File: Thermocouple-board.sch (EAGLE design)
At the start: 78 parts, among them J1 RJ45, J11 1X2-3.5MM, J12 1X2-3.5MM, J13 1X2-3.5MM, J14 1X2-3.5MM, J2 RJ45, J3 1981584-1, J4 2.1MMJACKTHM, J5 ST-LINK, J6 HEADER-1X3, J7 HEADER-1X2, SW1 PUSHBUTTON, SW2 PUSHBUTTON, U1 STM32F042K4, U10 MAX31855, U11 MAX31855, U12 MAX31855, U13 MAX31855, U20 EEPROM-I2C, U21 EEPROM-I2C, U30 ST3485, U31 ST3485, U40 LP298XS, X1 NX3225GD

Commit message: WIP on larger MTG holes
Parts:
- added MH1, MH2, MH3, MH4: 4-40, Thermocouple-board:MTG_HOLE_4-40
- added U$3, U$6: MOUNTINGHOLE2.0, microbuilder:MOUNTINGHOLE2.0
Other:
- note added: "CENTER POSITIVE"
- note removed: "PWR ONLY"
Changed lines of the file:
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@@
 <part name="J6" library="Thermocouple-board" deviceset="HEADER-1X3" device=""/>
 <part name="C42" library="adafruit" deviceset="C-US" device="C0805K" value="10uF"/>
+<part name="MH1" library="Thermocouple-board" deviceset="MTG_HOLE" device="_4-40" value="4-40"/>
+<part name="MH2" library="Thermocouple-board" deviceset="MTG_HOLE" device="_4-40" value="4-40"/>
+<part name="MH3" library="Thermocouple-board" deviceset="MTG_HOLE" device="_4-40" value="4-40"/>
+<part name="MH4" library="Thermocouple-board" deviceset="MTG_HOLE" device="_4-40" value="4-40"/>
+<part name="U$3" library="microbuilder" deviceset="MOUNTINGHOLE" device="2.0"/>
+<part name="U$6" library="microbuilder" deviceset="MOUNTINGHOLE" device="2.0"/>
 </parts>
 <sheets>
@@
 8. DC-</text>
 <text x="-43.18" y="101.6" size="1.778" layer="91">ETHERNET</text>
-<text x="147.32" y="147.32" size="1.778" layer="91">PWR ONLY</text>
 <text x="73.66" y="127" size="1.778" layer="91">MTG HOLES</text>
 <text x="40.64" y="132.08" size="1.778" layer="91">POWER SELECT</text>
+<text x="-25.4" y="132.08" size="1.778" layer="91">CENTER POSITIVE</text>
 </plain>
 <instances>
@@
 <attribute name="VALUE" x="28.956" y="38.989" size="1.778" layer="96"/>
 </instance>
+<instance part="MH1" gate="G$1" x="88.9" y="121.92" smashed="yes">
+<attribute name="NAME" x="86.36" y="125.73" size="1.27" layer="95"/>
+<attribute name="VALUE" x="86.36" y="116.84" size="1.27" layer="96"/>
+</instance>
+<instance part="MH2" gate="G$1" x="96.52" y="121.92" smashed="yes">
+<attribute name="NAME" x="93.98" y="125.73" size="1.27" layer="95"/>
+<attribute name="VALUE" x="93.98" y="116.84" size="1.27" layer="96"/>
+</instance>
+<instance part="MH3" gate="G$1" x="104.14" y="121.92" smashed="yes">
+<attribute name="NAME" x="101.6" y="125.73" size="1.27" layer="95"/>
+<attribute name="VALUE" x="101.6" y="116.84" size="1.27" layer="96"/>
+</instance>
+<instance part="MH4" gate="G$1" x="111.76" y="121.92" smashed="yes">
+<attribute name="NAME" x="109.22" y="125.73" size="1.27" layer="95"/>
+<attribute name="VALUE" x="109.22" y="116.84" size="1.27" layer="96"/>
+</instance>
+<instance part="U$3" gate="G$1" x="76.2" y="111.76" smashed="yes"/>
+<instance part="U$6" gate="G$1" x="81.28" y="111.76" smashed="yes"/>
 </instances>
 <busses>

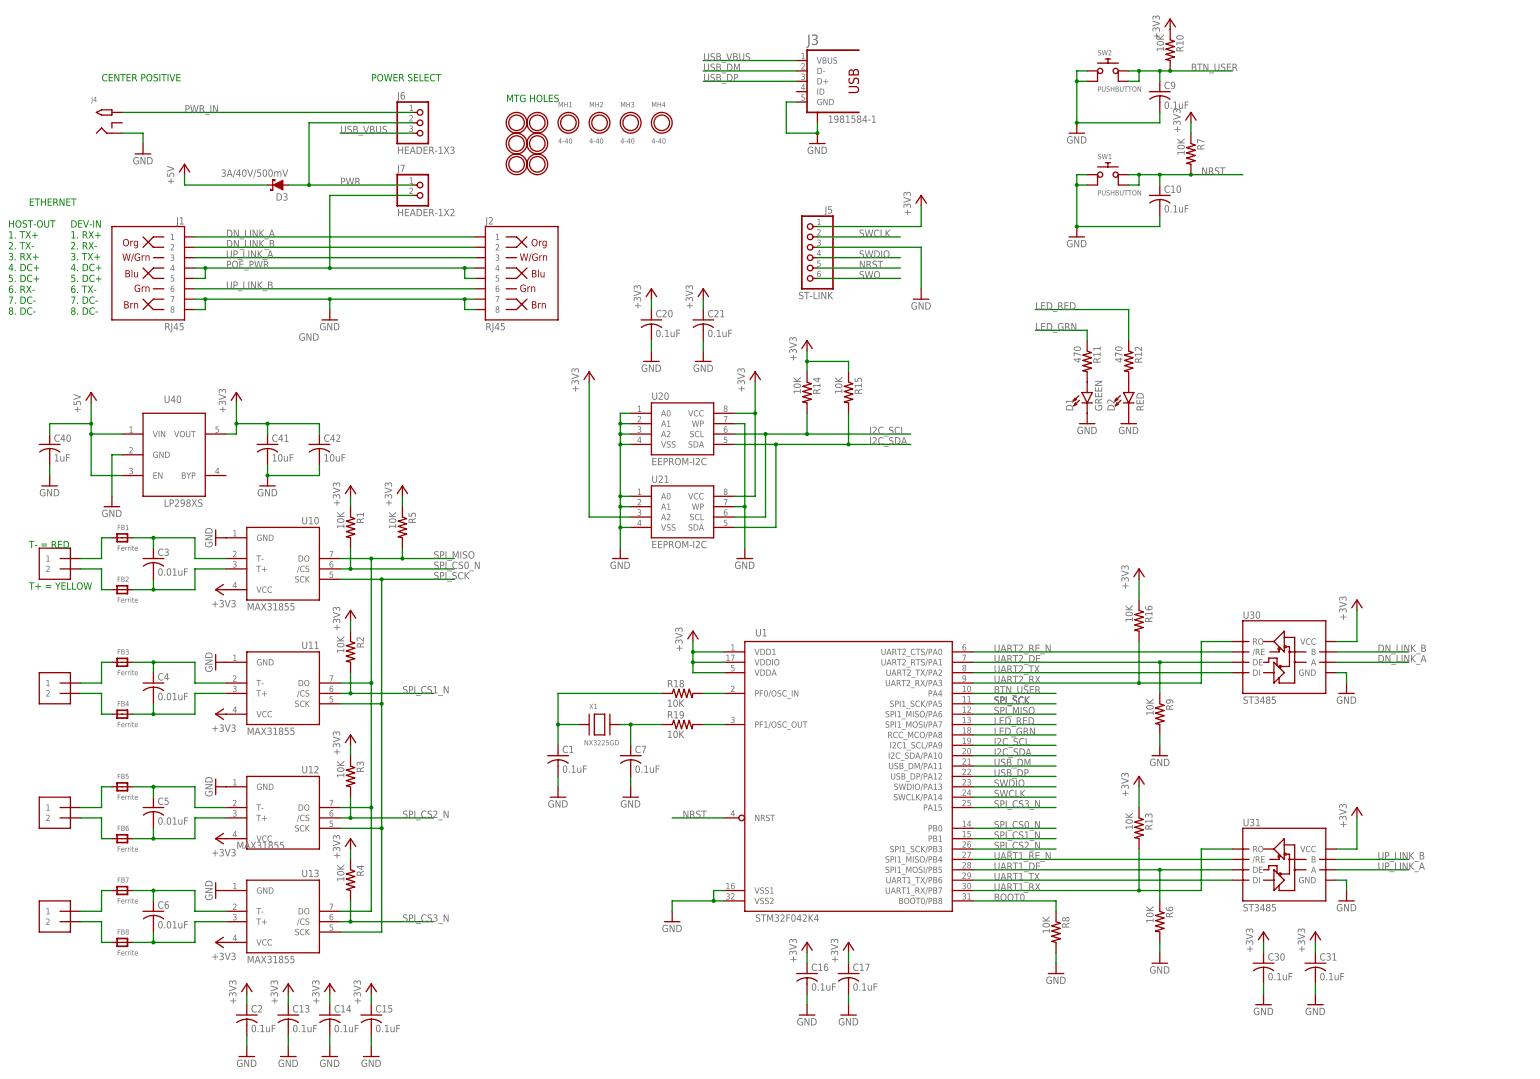
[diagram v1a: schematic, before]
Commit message: Reconfigured UARTs for FTDI cable
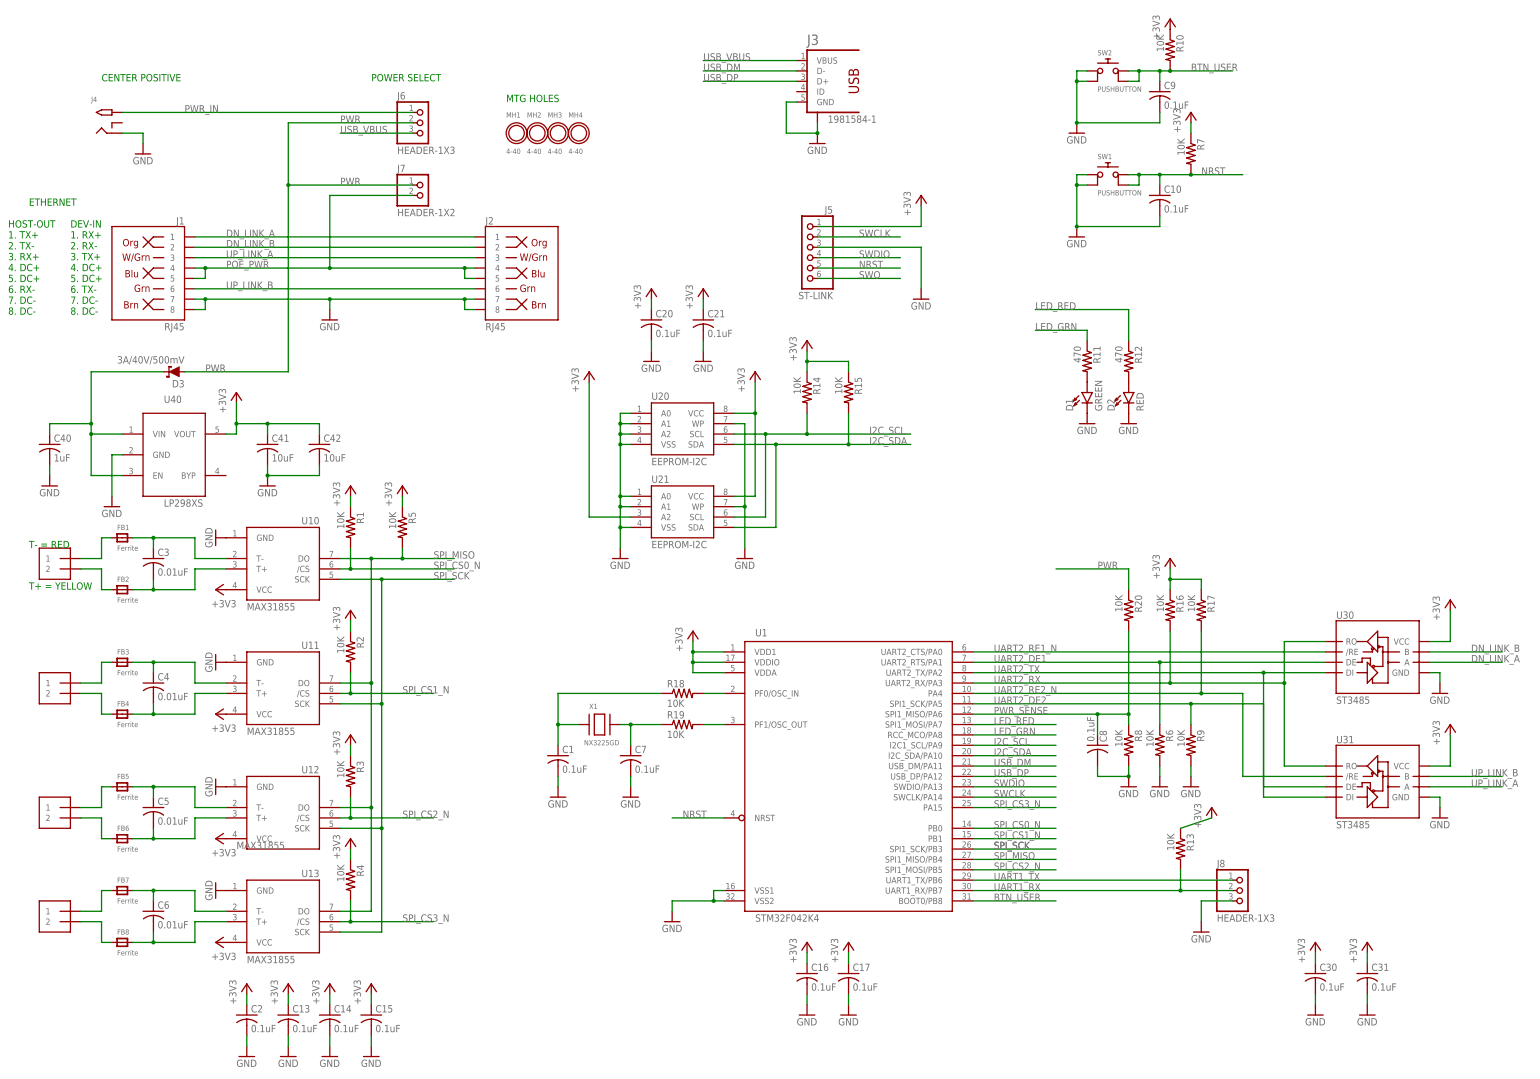
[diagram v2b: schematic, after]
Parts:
- removed U$1, U$2, U$3, U$4, U$5, U$6: MOUNTINGHOLE2.0, microbuilder:MOUNTINGHOLE2.0
- added C8: 0.1uF, adafruit:C-USC0805K
- added J8: HEADER-1X3, Thermocouple-board:HEADER-1X3
- added R17, R20: 10K, adafruit:R-US_R0805
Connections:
- net +5V renamed N$21
- net UART2_RE_N renamed UART2_RE1_N
- removed net BOOT0: R8.1, U1.BOOT0/PB8
- removed net UART1_DE: R6.1, U1.SPI1_MOSI/PB5, U31.DE
- removed net UART1_RE_N: U1.SPI1_MISO/PB4, U31./RE
- removed net UART2_DE: R9.1, U1.UART2_RTS/PA1, U30.DE
- new net PWR_SENSE: C8.1, R20.2, R8.1, U1.SPI1_MISO/PA6
- new net UART2_DE1: R6.1, U1.UART2_RTS/PA1, U30.DE
- new net UART2_DE2: R9.1, U1.SPI1_SCK/PA5, U31.DE
- new net UART2_RE2_N: R17.2, U1.PA4, U31./RE
- net +3V3: now also R17.1
- net BTN_USER: now also U1.BOOT0/PB8; no longer U1.PA4
- net GND: now also C8.2, J8.3
- net PWR: now also R20.1
- net SPI_CS2_N: now also U1.SPI1_MOSI/PB5; no longer U1.SPI1_SCK/PB3
- net SPI_MISO: now also U1.SPI1_MISO/PB4; no longer U1.SPI1_MISO/PA6
- net SPI_SCK: now also U1.SPI1_SCK/PB3; no longer U1.SPI1_SCK/PA5
- net UART1_RX: now also J8.2; no longer U31.RO
- net UART1_TX: now also J8.1; no longer U31.DI
- net UART2_RX: now also U31.RO
- net UART2_TX: now also U31.DI
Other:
- moved on the sheet: C30, C31, D3, MH1, MH2, MH3, MH4, R13, R16, R6, R8, R9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

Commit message: Finish routing.
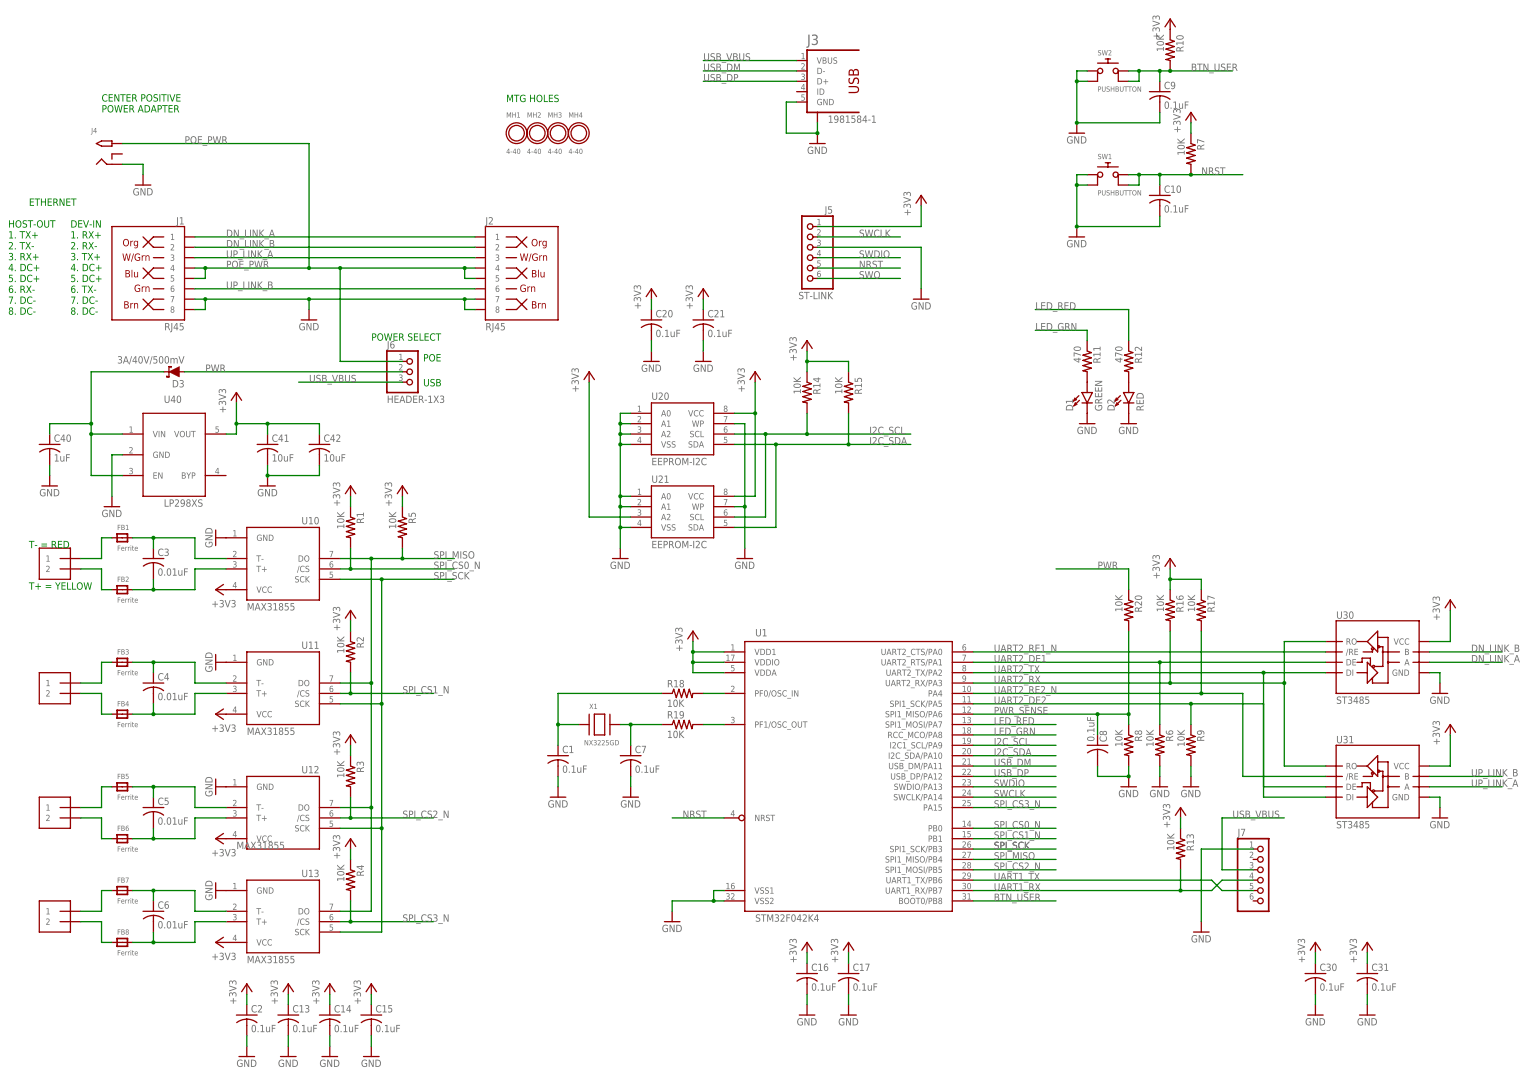
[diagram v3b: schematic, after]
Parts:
- removed J8: HEADER-1X3, Thermocouple-board:HEADER-1X3
- J7: value HEADER-1X2 -> (none); device Thermocouple-board:HEADER-1X2 -> Thermocouple-board:HEADER-1X6
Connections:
- removed net PWR_IN: J4.TIP, J6.1
- net GND: now also J7.1; no longer J8.3
- net POE_PWR: now also J4.TIP, J6.1; no longer J7.2
- net PWR: no longer J7.1
- net UART1_RX: now also J7.4; no longer J8.2
- net UART1_TX: now also J7.5; no longer J8.1
- net USB_VBUS: now also J7.3
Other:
- note added: "CENTER POSITIVE POWER ADAPTER"
- note added: "POE"
- note added: "USB"
- note removed: "CENTER POSITIVE"
- moved on the sheet: J4, J6

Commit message: Finish cleanup. Added schem frame.
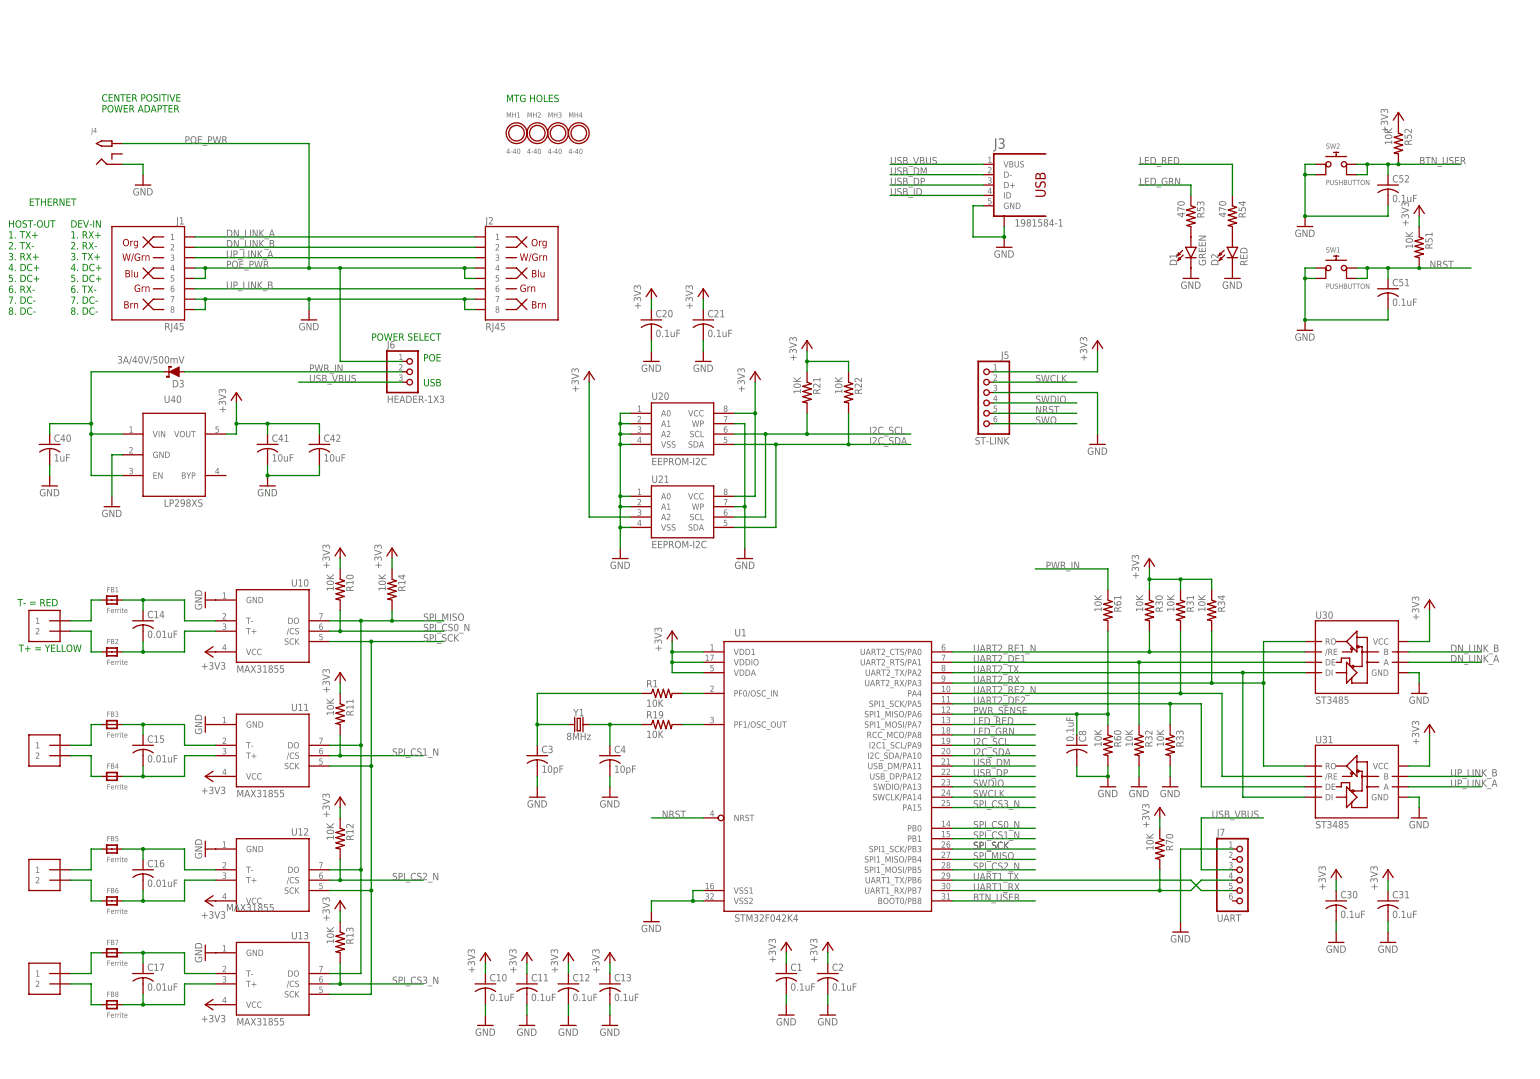
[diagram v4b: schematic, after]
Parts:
- removed C5, C6: 0.01uF, adafruit:C-USC0805K
- removed C7, C9: 0.1uF, adafruit:C-USC0805K
- removed J14: 1X2-3.5MM, Thermocouple-board:1X2-3.5MM
- removed R16, R17, R18, R2, R20, R3, R4, R5, R6, R7, R8, R9: 10K, adafruit:R-US_R0805
- removed X1: NX3225GD, Thermocouple-board:NX3225GD
- added C11, C12, C51, C52: 0.1uF, adafruit:C-USC0805K
- added J10: 1X2-3.5MM, Thermocouple-board:1X2-3.5MM
- added R21, R30, R31, R32, R33, R34, R51, R52, R60, R61, R70: 10K, adafruit:R-US_R0805
- added R53, R54: 470, adafruit:R-US_R0805
- added Y1: 8MHz, SparkFun-Clocks:CRYSTAL-8MHZSMD-HC49UP
- C14, C15, C16, C17: value 0.1uF -> 0.01uF
- C3, C4: value 0.01uF -> 10pF
- J7: value (none) -> UART
- R11, R12: value 470 -> 10K
- renumbered R15 to R22
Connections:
- removed net PWR: D3.A, J6.2, R20.1
- new net PWR_IN: D3.A, J6.2, R61.1
- new net USB_ID: J3.ID
- net +3V3: now also C1.1, C10.1, C11.1, C12.1, R11.1, R12.1, R21.1, R30.1, R31.1, R34.1, R51.1, R52.1, R70.1; no longer C14.1, C15.1, C16.1, C17.1, R1.1, R16.1, R17.1, R2.1, R3.1, R4.1, R5.1, R7.1
- net BTN_USER: now also C52.1, R52.2; no longer C9.1, R10.2
- net GND: now also C11.2, C12.2, C3.2, C4.2, C51.2, C52.2, R32.2, R33.2, R60.2; no longer C14.2, C15.2, C16.2, C17.2, C7.2, C9.2, R6.2, R8.2, R9.2
- net I2C_SCL: now also R21.2; no longer R14.2
- net LED_GRN: now also R53.1; no longer R11.1
- net LED_RED: now also R54.1; no longer R12.1
- net N$1: now also J10.1; no longer J11.1
- net N$10: now also C15.2; no longer C4.2
- net N$11: now also J12.1; no longer J13.1
- net N$12: now also C16.1; no longer C5.1
- net N$13: now also J12.2; no longer J13.2
- net N$14: now also C16.2; no longer C5.2
- net N$15: now also J13.1; no longer J14.1
- net N$16: now also C17.1; no longer C6.1
- net N$17: now also J13.2; no longer J14.2
- net N$18: now also C17.2; no longer C6.2
- net N$19: now also C4.1, Y1.2; no longer C7.1, X1.X2
- net N$2: now also R1.2; no longer R18.2
- net N$20: now also C3.1, R1.1, Y1.1; no longer C1.1, R18.1, X1.X1
- net N$25: now also R53.2; no longer R11.2
- net N$26: now also R54.2; no longer R12.2
- net N$4: now also C14.1; no longer C3.1
- net N$5: now also J10.2; no longer J11.2
- net N$6: now also C14.2; no longer C3.2
- net N$7: now also J11.1; no longer J12.1
- net N$8: now also C15.1; no longer C4.1
- net N$9: now also J11.2; no longer J12.2
- net NRST: now also C51.1, R51.2; no longer C10.1, R7.2
- net PWR_SENSE: now also R60.1, R61.2; no longer R20.2, R8.1
- net SPI_CS0_N: now also R10.2; no longer R1.2
- net SPI_CS1_N: now also R11.2; no longer R2.2
- net SPI_CS2_N: now also R12.2; no longer R3.2
- net SPI_CS3_N: now also R13.2; no longer R4.2
- net SPI_MISO: now also R14.2; no longer R5.2
- net UART1_RX: now also R70.2; no longer R13.2
- net UART2_DE1: now also R32.1; no longer R6.1
- net UART2_DE2: now also R33.1; no longer R9.1
- net UART2_RE1_N: now also R30.2
- net UART2_RE2_N: now also R31.2; no longer R17.2
- net UART2_RX: now also R34.2; no longer R16.2
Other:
- moved on the sheet: C1, C10, C13, C14, C15, C16, C17, C2, C3, C30, C31, C4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
